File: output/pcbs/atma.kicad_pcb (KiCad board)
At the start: 2 copper layers, 99.8 x 100 mm, 24 parts

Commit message: more ergonomic 36-key version
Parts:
- moved ? 97.7 mm to (154.3, 172.4)
- moved _6 71.0 mm to (154.3, 172.4)
- moved _4 60.1 mm to (218.9, 123.8)
- moved _5 51.3 mm to (237.9, 171.4)
- moved ? 25.4 mm to (247.5, 121.9)
- moved S16 15.9 mm to (209.4, 181.0)
- moved S17 15.9 mm to (228.4, 181.0)
- moved S18 15.9 mm to (247.4, 181.0)
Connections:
- ? pad 1: matrix_pinky_bottom -> matrix_pinky_top
- ? pad 10: GP9 -> matrix_index_top
- ? pad 11: matrix_middle_top -> matrix_index_home
- ? pad 12: matrix_inner_bottom -> matrix_index_bottom
- ? pad 13: matrix_inner_home -> GP12
- ? pad 14: matrix_inner_top -> GP13
- ? pad 15: matrix_index_top -> matrix_inner_bottom
- ? pad 16: matrix_index_home -> matrix_inner_home
- ? pad 17: matrix_index_bottom -> matrix_inner_top
- ? pad 18: thumbfan_far_home -> thumbfan_near_home
- ? pad 20: thumbfan_near_home -> thumbfan_far_home
- ? pad 3: matrix_pinky_top -> matrix_pinky_bottom
- ? pad 4: matrix_ring_top -> matrix_ring_bottom
- ? pad 6: matrix_ring_bottom -> matrix_ring_top
- ? pad 7: matrix_middle_bottom -> matrix_middle_top
- ? pad 9: GP8 -> matrix_middle_bottom
- ? pad 3: GP8 -> GP12
- ? pad 4: GP8 -> GP12
- ? pad 5: GP9 -> GP13
- ? pad 6: GP9 -> GP13
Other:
- board size 99.8 x 100 mm -> 114.1 x 85.7 mm

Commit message: outline tweaks
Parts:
- removed _6: , MountingHole_2.2mm_M2_Pad_Via
- moved ? 35.2 mm to (247.5, 157.2)
- moved _5 19.6 mm to (218.9, 166.7)
- moved _3 19.1 mm to (161.9, 142.9)
- moved _4 19.0 mm to (199.9, 123.8)
- moved S16 4.76 mm to (209.4, 176.2)
- moved S17 4.76 mm to (228.4, 176.2)
- moved S18 4.76 mm to (247.4, 176.2)
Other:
- board size 114.1 x 85.7 mm -> 114.1 x 81 mm
- board text added: "JLCJLCJLCJLC"
- board text added: "atma v0.2.0"
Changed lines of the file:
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@@
           )
       (module MX (layer F.Cu)
-      (at 209.4 180.975 0)
+      (at 209.4 176.2125 0)
       (fp_text reference "S16" (at 0 0) (layer F.SilkS) hide (effects (font (size 1.27 1.27) (thickness 0.15))))
       (fp_text value "" (at 0 0) (layer F.SilkS) hide (effects (font (size 1.27 1.27) (thickness 0.15))))
@@
           )
       (module MX (layer F.Cu)
-      (at 228.4 180.975 0)
+      (at 228.4 176.2125 0)
       (fp_text reference "S17" (at 0 0) (layer F.SilkS) hide (effects (font (size 1.27 1.27) (thickness 0.15))))
       (fp_text value "" (at 0 0) (layer F.SilkS) hide (effects (font (size 1.27 1.27) (thickness 0.15))))
@@
           )
       (module MX (layer F.Cu)
-      (at 247.4 180.975 0)
+      (at 247.4 176.2125 0)
       (fp_text reference "S18" (at 0 0) (layer F.SilkS) hide (effects (font (size 1.27 1.27) (thickness 0.15))))
       (fp_text value "" (at 0 0) (layer F.SilkS) hide (effects (font (size 1.27 1.27) (thickness 0.15))))
@@
     )
     (module "44144-0003" (layer F.Cu)
-      (at 247.45000000000002 121.91999999999999 180)
+      (at 247.45000000000002 157.1625 180)
       (fp_line (start -7.62 0) (end 7.62 0) (layer F.Fab) (width 0.2))
       (fp_line (start 7.62 0) (end 7.62 16.89) (layer F.Fab) (width 0.2))
@@
     )
     (module "MountingHole_2.2mm_M2_Pad_Via" (version 20210722) (generator pcbnew) (layer "F.Cu")
-      (at 161.875 123.82499999999999 0)
+      (at 161.925 142.875 0)
       (fp_text reference "_3" (at 0 -3.2) (layer "F.SilkS") hide
         (effects (font (size 1 1) (thickness 0.15)))
@@
     )
     (module "MountingHole_2.2mm_M2_Pad_Via" (version 20210722) (generator pcbnew) (layer "F.Cu")
-      (at 218.925 123.82499999999999 0)
+      (at 199.925 123.82499999999999 0)
       (fp_text reference "_4" (at 0 -3.2) (layer "F.SilkS") hide
         (effects (font (size 1 1) (thickness 0.15)))
@@
     )
     (module "MountingHole_2.2mm_M2_Pad_Via" (version 20210722) (generator pcbnew) (layer "F.Cu")
-      (at 237.925 171.45 0)
+      (at 218.925 166.6875 0)
       (fp_text reference "_5" (at 0 -3.2) (layer "F.SilkS") hide
         (effects (font (size 1 1) (thickness 0.15)))
@@
       (pad "1" thru_hole circle locked (at 0 -1.65) (size 0.7 0.7) (drill 0.4) (layers *.Cu *.Mask))
     )
-    (module "MountingHole_2.2mm_M2_Pad_Via" (version 20210722) (generator pcbnew) (layer "F.Cu")
-      (at 154.305 172.4025 0)
-      (fp_text reference "_6" (at 0 -3.2) (layer "F.SilkS") hide
-        (effects (font (size 1 1) (thickness 0.15)))
-      )
-      (fp_circle (center 0 0) (end 2.45 0) (layer "F.CrtYd") (width 0.05) (fill none))
-      (pad "1" thru_hole circle locked (at 1.166726 1.166726) (size 0.7 0.7) (drill 0.4) (layers *.Cu *.Mask))
-      (pad "1" thru_hole circle locked (at 0 0) (size 4.4 4.4) (drill 2.2) (layers *.Cu *.Mask))
-      (pad "1" thru_hole circle locked (at 0 1.65) (size 0.7 0.7) (drill 0.4) (layers *.Cu *.Mask))
-      (pad "1" thru_hole circle locked (at 1.166726 -1.166726) (size 0.7 0.7) (drill 0.4) (layers *.Cu *.Mask))
-      (pad "1" thru_hole circle locked (at -1.65 0) (size 0.7 0.7) (drill 0.4) (layers *.Cu *.Mask))
-      (pad "1" thru_hole circle locked (at -1.166726 -1.166726) (size 0.7 0.7) (drill 0.4) (layers *.Cu *.Mask))
-      (pad "1" thru_hole circle locked (at -1.166726 1.166726) (size 0.7 0.7) (drill 0.4) (layers *.Cu *.Mask))
-      (pad "1" thru_hole circle locked (at 1.65 0) (size 0.7 0.7) (drill 0.4) (layers *.Cu *.Mask))
-      (pad "1" thru_hole circle locked (at 0 -1.65) (size 0.7 0.7) (drill 0.4) (layers *.Cu *.Mask))
-    )
-            (gr_line (start 142.875 182.97549871897368) (end 142.875 106.77499999999999) (angle 90) (layer Edge.Cuts) (width 0.15))
-(gr_line (start 144.875 104.77499999999999) (end 254.97383309877515 104.77499999999999) (angle 90) (layer Edge.Cuts) (width 0.15))
-(gr_line (start 256.97383279871684 106.77616660005879) (end 256.92616584041997 188.5011665999773) (angle 90) (layer Edge.Cuts) (width 0.15))
-(gr_line (start 254.9261661404783 190.5) (end 199.9750127766405 190.5) (angle 90) (layer Edge.Cuts) (width 0.15))
-(gr_line (start 199.77548676770925 190.49002248907823) (end 144.67547399106874 184.96552120805188) (angle 90) (layer Edge.Cuts) (width 0.15))
+            (gr_text "atma v0.2.0" (at 180.925 123.82499999999999 0) (layer F.SilkS)
+                (effects (font (size 1 1) (thickness 0.15)) )
+            )
+            (gr_text "JLCJLCJLCJLC" (at 180.925 142.875 0) (layer F.SilkS)
+                (effects (font (size 1 1) (thickness 0.15)) )
+            )
+            (gr_line (start 142.875 183.7375) (end 142.875 106.77499999999999) (angle 90) (layer Edge.Cuts) (width 0.15))
+(gr_line (start 144.875 104.77499999999999) (end 245.9413971571429 104.77499999999999) (angle 90) (layer Edge.Cuts) (width 0.15))
+(gr_line (start 247.8644450760108 106.22555776603781) (end 256.8977538164621 137.84213835761727) (angle 90) (layer Edge.Cuts) (width 0.15))
+(gr_line (start 256.97470479748904 138.39368039168767) (end 256.92709753301824 183.73959980011568) (angle 90) (layer Edge.Cuts) (width 0.15))
+(gr_line (start 144.875 185.7375) (end 254.92709863312336 185.7375) (angle 90) (layer Edge.Cuts) (width 0.15))
 (gr_arc (start 144.875 106.77499999999999) (end 144.875 104.77499999999999) (angle -90) (layer Edge.Cuts) (width 0.15))
-(gr_arc (start 254.97383309877515 106.77499999999999) (end 256.97383279877516 106.7761666) (angle -90.03342063109807) (layer Edge.Cuts) (width 0.15))
-(gr_arc (start 254.9261661404783 188.5) (end 254.9261661404783 190.5) (angle -89.96657937123672) (layer Edge.Cuts) (width 0.15))
-(gr_arc (start 199.9750127766405 188.5) (end 199.77548677664052 190.4900225) (angle -5.725523291754314) (layer Edge.Cuts) (width 0.15))
-(gr_arc (start 144.875 182.97549871897368) (end 142.875 182.97549871897368) (angle -84.27447670824557) (layer Edge.Cuts) (width 0.15))
+(gr_arc (start 245.9413971571429 106.77499999999999) (end 247.8644450571429 106.22555779999999) (angle -74.05460488609745) (layer Edge.Cuts) (width 0.15))
+(gr_arc (start 254.97470589759416 138.39158059157955) (end 256.97470479759414 138.39368039157955) (angle -16.00554996689867) (layer Edge.Cuts) (width 0.15))
+(gr_arc (start 254.92709863312336 183.73749999998836) (end 254.92709863312336 185.73749999998836) (angle -89.93984514645598) (layer Edge.Cuts) (width 0.15))
+(gr_arc (start 144.875 183.7375) (end 142.875 183.7375) (angle -90) (layer Edge.Cuts) (width 0.15))
 )

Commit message: outline tweaks, reroute
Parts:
- moved ? 2.86 mm to (247.5, 160.0)
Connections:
- ? pad 10: matrix_index_top -> matrix_index_bottom
- ? pad 12: matrix_index_bottom -> matrix_index_top
- ? pad 15: matrix_inner_bottom -> matrix_inner_top
- ? pad 17: matrix_inner_top -> matrix_inner_bottom
- ? pad 3: GP12 -> GP13
- ? pad 4: GP12 -> GP13
- ? pad 5: GP13 -> GP12
- ? pad 6: GP13 -> GP12
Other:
- outline, holes or cut-outs redrawn
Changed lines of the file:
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@@
       (pad 8 thru_hole oval (at 7.62 7.62 270) (size 2.5 1.5) (drill 1 (offset -0.5 0)) (layers *.Cu *.Mask) (net 9 "matrix_middle_home"))
       (pad 9 thru_hole oval (at 7.62 10.16 270) (size 2.5 1.5) (drill 1 (offset -0.5 0)) (layers *.Cu *.Mask) (net 8 "matrix_middle_bottom"))
-      (pad 10 thru_hole oval (at 5.08 10.16 180) (size 2.5 1.5) (drill 1 (offset -0.5 0)) (layers *.Cu *.Mask) (net 13 "matrix_index_top"))
+      (pad 10 thru_hole oval (at 5.08 10.16 180) (size 2.5 1.5) (drill 1 (offset -0.5 0)) (layers *.Cu *.Mask) (net 11 "matrix_index_bottom"))
       (pad 11 thru_hole oval (at 2.54 10.16 180) (size 2.5 1.5) (drill 1 (offset -0.5 0)) (layers *.Cu *.Mask) (net 12 "matrix_index_home"))
-      (pad 12 thru_hole oval (at 0 10.16 180) (size 2.5 1.5) (drill 1 (offset -0.5 0)) (layers *.Cu *.Mask) (net 11 "matrix_index_bottom"))
+      (pad 12 thru_hole oval (at 0 10.16 180) (size 2.5 1.5) (drill 1 (offset -0.5 0)) (layers *.Cu *.Mask) (net 13 "matrix_index_top"))
       (pad 13 thru_hole oval (at -2.54 10.16 180) (size 2.5 1.5) (drill 1 (offset -0.5 0)) (layers *.Cu *.Mask) (net 20 "GP12"))
       (pad 14 thru_hole oval (at -5.08 10.16 180) (size 2.5 1.5) (drill 1 (offset -0.5 0)) (layers *.Cu *.Mask) (net 21 "GP13"))
-      (pad 15 thru_hole oval (at -7.62 10.16 90) (size 2.5 1.5) (drill 1 (offset -0.5 0)) (layers *.Cu *.Mask) (net 14 "matrix_inner_bottom"))
+      (pad 15 thru_hole oval (at -7.62 10.16 90) (size 2.5 1.5) (drill 1 (offset -0.5 0)) (layers *.Cu *.Mask) (net 16 "matrix_inner_top"))
       (pad 16 thru_hole oval (at -7.62 7.62 90) (size 2.5 1.5) (drill 1 (offset -0.5 0)) (layers *.Cu *.Mask) (net 15 "matrix_inner_home"))
-      (pad 17 thru_hole oval (at -7.62 5.08 90) (size 2.5 1.5) (drill 1 (offset -0.5 0)) (layers *.Cu *.Mask) (net 16 "matrix_inner_top"))
+      (pad 17 thru_hole oval (at -7.62 5.08 90) (size 2.5 1.5) (drill 1 (offset -0.5 0)) (layers *.Cu *.Mask) (net 14 "matrix_inner_bottom"))
       (pad 18 thru_hole oval (at -7.62 2.54 90) (size 2.5 1.5) (drill 1 (offset -0.5 0)) (layers *.Cu *.Mask) (net 17 "thumbfan_near_home"))
       (pad 19 thru_hole oval (at -7.62 0 90) (size 2.5 1.5) (drill 1 (offset -0.5 0)) (layers *.Cu *.Mask) (net 18 "thumbfan_home_home"))
@@
     )
     (module "44144-0003" (layer F.Cu)
-      (at 247.45000000000002 157.1625 180)
+      (at 247.45000000000002 160.02 180)
       (fp_line (start -7.62 0) (end 7.62 0) (layer F.Fab) (width 0.2))
       (fp_line (start 7.62 0) (end 7.62 16.89) (layer F.Fab) (width 0.2))
@@
       (pad 1 smd rect (at -4.445 -0.83 180) (size 0.64 2.54) (layers F.Cu F.Paste F.Mask) (net 22 "3V3"))
       (pad 2 smd rect (at -3.175 -0.83 180) (size 0.64 2.54) (layers F.Cu F.Paste F.Mask) (net 2 "GND"))
-      (pad 3 smd rect (at -1.905 -0.83 180) (size 0.64 2.54) (layers F.Cu F.Paste F.Mask) (net 20 "GP12"))
-      (pad 4 smd rect (at -0.635 -0.83 180) (size 0.64 2.54) (layers F.Cu F.Paste F.Mask) (net 20 "GP12"))
-      (pad 5 smd rect (at 0.635 -0.83 180) (size 0.64 2.54) (layers F.Cu F.Paste F.Mask) (net 21 "GP13"))
-      (pad 6 smd rect (at 1.905 -0.83 180) (size 0.64 2.54) (layers F.Cu F.Paste F.Mask) (net 21 "GP13"))
+      (pad 3 smd rect (at -1.905 -0.83 180) (size 0.64 2.54) (layers F.Cu F.Paste F.Mask) (net 21 "GP13"))
+      (pad 4 smd rect (at -0.635 -0.83 180) (size 0.64 2.54) (layers F.Cu F.Paste F.Mask) (net 21 "GP13"))
+      (pad 5 smd rect (at 0.635 -0.83 180) (size 0.64 2.54) (layers F.Cu F.Paste F.Mask) (net 20 "GP12"))
+      (pad 6 smd rect (at 1.905 -0.83 180) (size 0.64 2.54) (layers F.Cu F.Paste F.Mask) (net 20 "GP12"))
       (pad 7 smd rect (at 3.175 -0.83 180) (size 0.64 2.54) (layers F.Cu F.Paste F.Mask) (net 2 "GND"))
       (pad 8 smd rect (at 4.445 -0.83 180) (size 0.64 2.54) (layers F.Cu F.Paste F.Mask) (net 22 "3V3"))
@@
       (pad 1 smd rect (at -4.445 -0.83 180) (size 0.64 2.54) (layers B.Cu B.Paste B.Mask) (net 22 "3V3"))
       (pad 2 smd rect (at -3.175 -0.83 180) (size 0.64 2.54) (layers B.Cu B.Paste B.Mask) (net 2 "GND"))
-      (pad 3 smd rect (at -1.905 -0.83 180) (size 0.64 2.54) (layers B.Cu B.Paste B.Mask) (net 20 "GP12"))
-      (pad 4 smd rect (at -0.635 -0.83 180) (size 0.64 2.54) (layers B.Cu B.Paste B.Mask) (net 20 "GP12"))
-      (pad 5 smd rect (at 0.635 -0.83 180) (size 0.64 2.54) (layers B.Cu B.Paste B.Mask) (net 21 "GP13"))
-      (pad 6 smd rect (at 1.905 -0.83 180) (size 0.64 2.54) (layers B.Cu B.Paste B.Mask) (net 21 "GP13"))
+      (pad 3 smd rect (at -1.905 -0.83 180) (size 0.64 2.54) (layers B.Cu B.Paste B.Mask) (net 21 "GP13"))
+      (pad 4 smd rect (at -0.635 -0.83 180) (size 0.64 2.54) (layers B.Cu B.Paste B.Mask) (net 21 "GP13"))
+      (pad 5 smd rect (at 0.635 -0.83 180) (size 0.64 2.54) (layers B.Cu B.Paste B.Mask) (net 20 "GP12"))
+      (pad 6 smd rect (at 1.905 -0.83 180) (size 0.64 2.54) (layers B.Cu B.Paste B.Mask) (net 20 "GP12"))
       (pad 7 smd rect (at 3.175 -0.83 180) (size 0.64 2.54) (layers B.Cu B.Paste B.Mask) (net 2 "GND"))
       (pad 8 smd rect (at 4.445 -0.83 180) (size 0.64 2.54) (layers B.Cu B.Paste B.Mask) (net 22 "3V3"))
@@
                 (effects (font (size 1 1) (thickness 0.15)) )
             )
-            (gr_line (start 142.875 183.7375) (end 142.875 106.77499999999999) (angle 90) (layer Edge.Cuts) (width 0.15))
-(gr_line (start 144.875 104.77499999999999) (end 245.9413971571429 104.77499999999999) (angle 90) (layer Edge.Cuts) (width 0.15))
-(gr_line (start 247.8644450760108 106.22555776603781) (end 256.8977538164621 137.84213835761727) (angle 90) (layer Edge.Cuts) (width 0.15))
-(gr_line (start 256.97470479748904 138.39368039168767) (end 256.92709753301824 183.73959980011568) (angle 90) (layer Edge.Cuts) (width 0.15))
-(gr_line (start 144.875 185.7375) (end 254.92709863312336 185.7375) (angle 90) (layer Edge.Cuts) (width 0.15))
-(gr_arc (start 144.875 106.77499999999999) (end 144.875 104.77499999999999) (angle -90) (layer Edge.Cuts) (width 0.15))
-(gr_arc (start 245.9413971571429 106.77499999999999) (end 247.8644450571429 106.22555779999999) (angle -74.05460488609745) (layer Edge.Cuts) (width 0.15))
-(gr_arc (start 254.97470589759416 138.39158059157955) (end 256.97470479759414 138.39368039157955) (angle -16.00554996689867) (layer Edge.Cuts) (width 0.15))
-(gr_arc (start 254.92709863312336 183.73749999998836) (end 254.92709863312336 185.73749999998836) (angle -89.93984514645598) (layer Edge.Cuts) (width 0.15))
-(gr_arc (start 144.875 183.7375) (end 142.875 183.7375) (angle -90) (layer Edge.Cuts) (width 0.15))
+            (gr_line (start 142.875 182.7375) (end 142.875 107.77499999999999) (angle 90) (layer Edge.Cuts) (width 0.15))
+(gr_line (start 145.875 104.77499999999999) (end 245.1870958 104.77499999999999) (angle 90) (layer Edge.Cuts) (width 0.15))
+(gr_line (start 248.07166761886796 106.95083666603784) (end 256.8591307152592 137.70695750340712) (angle 90) (layer Edge.Cuts) (width 0.15))
+(gr_line (start 256.9745571962861 138.53427053746418) (end 256.9281462995275 182.74064970004838) (angle 90) (layer Edge.Cuts) (width 0.15))
+(gr_line (start 145.875 185.7375) (end 253.92814799963259 185.7375) (angle 90) (layer Edge.Cuts) (width 0.15))
+(gr_arc (start 145.875 107.77499999999999) (end 145.875 104.77499999999999) (angle -90) (layer Edge.Cuts) (width 0.15))
+(gr_arc (start 245.1870958 107.77499999999999) (end 248.0716677 106.9508367) (angle -74.05460488609751) (layer Edge.Cuts) (width 0.15))
+(gr_arc (start 253.97455889639124 138.53112083736926) (end 256.97455719639123 138.53427053736925) (angle -16.005549966613025) (layer Edge.Cuts) (width 0.15))
+(gr_arc (start 253.92814799963259 182.73749999998836) (end 253.92814799963259 185.73749999998836) (angle -89.93984514795574) (layer Edge.Cuts) (width 0.15))
+(gr_arc (start 145.875 182.7375) (end 142.875 182.7375) (angle -90) (layer Edge.Cuts) (width 0.15))
 )

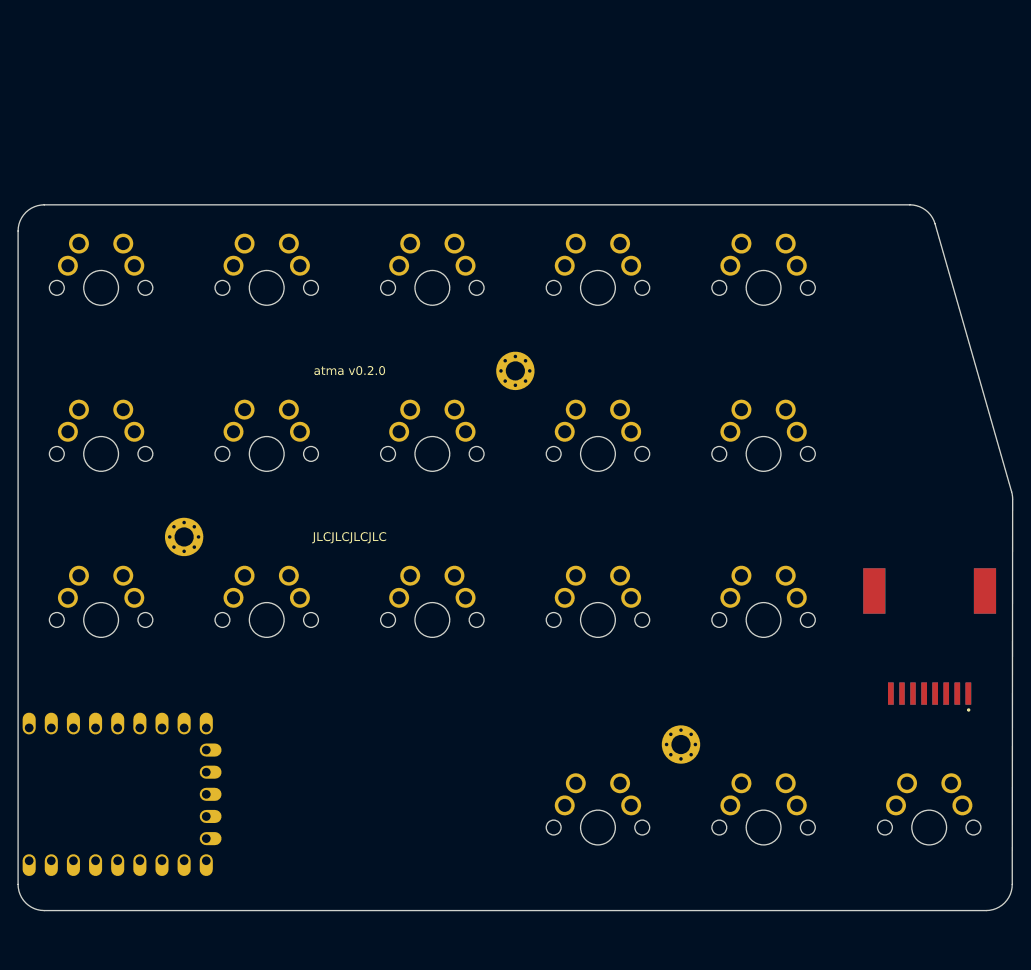
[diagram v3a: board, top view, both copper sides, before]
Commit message: small outline tweak
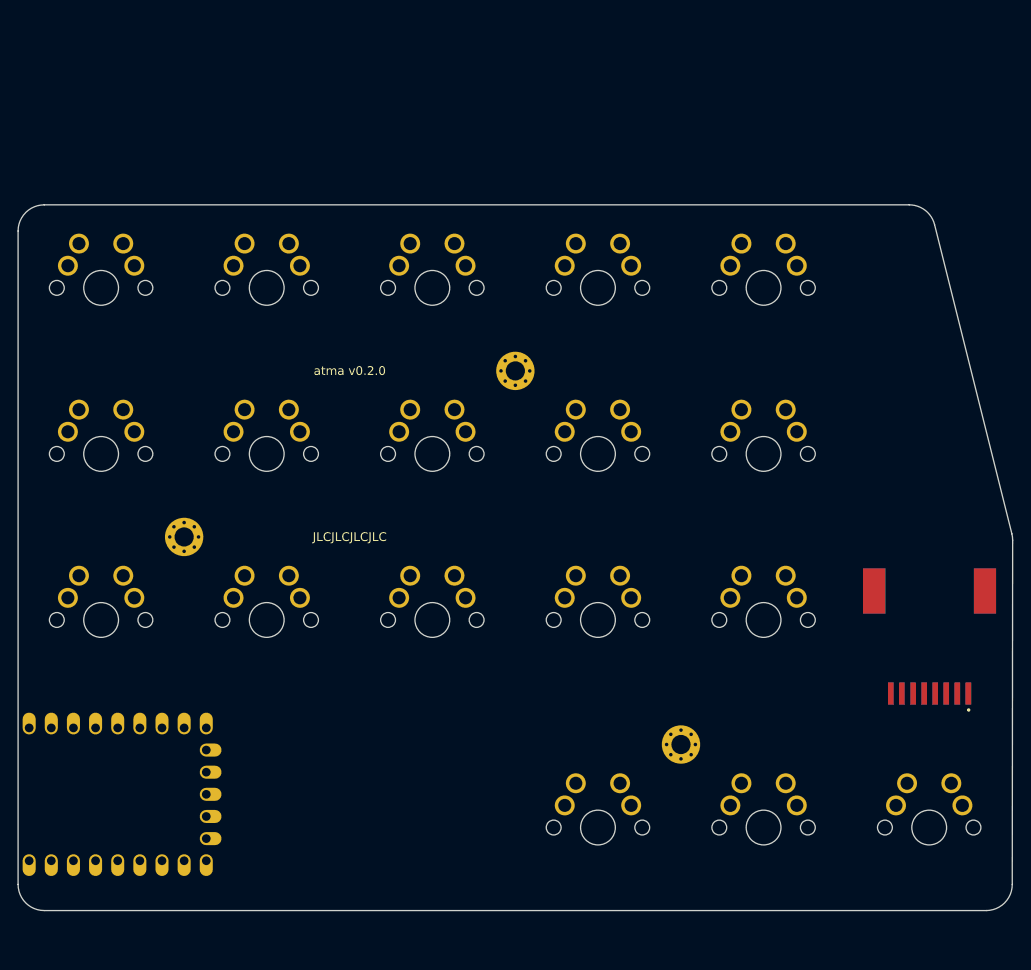
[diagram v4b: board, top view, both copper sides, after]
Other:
- outline, holes or cut-outs redrawn
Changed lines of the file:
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@@
             )
             (gr_line (start 142.875 182.7375) (end 142.875 107.77499999999999) (angle 90) (layer Edge.Cuts) (width 0.15))
-(gr_line (start 145.875 104.77499999999999) (end 245.1870958 104.77499999999999) (angle 90) (layer Edge.Cuts) (width 0.15))
-(gr_line (start 248.07166761886796 106.95083666603784) (end 256.8591307152592 137.70695750340712) (angle 90) (layer Edge.Cuts) (width 0.15))
-(gr_line (start 256.9745571962861 138.53427053746418) (end 256.9281462995275 182.74064970004838) (angle 90) (layer Edge.Cuts) (width 0.15))
-(gr_line (start 145.875 185.7375) (end 253.92814799963259 185.7375) (angle 90) (layer Edge.Cuts) (width 0.15))
+(gr_line (start 145.875 104.77499999999999) (end 245.107670775 104.77499999999999) (angle 90) (layer Edge.Cuts) (width 0.15))
+(gr_line (start 248.01809829852945 107.04739319411772) (end 256.8849966358661 142.51498654346437) (angle 90) (layer Edge.Cuts) (width 0.15))
+(gr_line (start 256.97456711245326 143.24609284946928) (end 256.9284954803149 182.74099950006348) (angle 90) (layer Edge.Cuts) (width 0.15))
+(gr_line (start 145.875 185.7375) (end 253.92849748019836 185.7375) (angle 90) (layer Edge.Cuts) (width 0.15))
 (gr_arc (start 145.875 107.77499999999999) (end 145.875 104.77499999999999) (angle -90) (layer Edge.Cuts) (width 0.15))
-(gr_arc (start 245.1870958 107.77499999999999) (end 248.0716677 106.9508367) (angle -74.05460488609751) (layer Edge.Cuts) (width 0.15))
-(gr_arc (start 253.97455889639124 138.53112083736926) (end 256.97455719639123 138.53427053736925) (angle -16.005549966613025) (layer Edge.Cuts) (width 0.15))
-(gr_arc (start 253.92814799963259 182.73749999998836) (end 253.92814799963259 185.73749999998836) (angle -89.93984514795574) (layer Edge.Cuts) (width 0.15))
+(gr_arc (start 245.107670775 107.77499999999999) (end 248.018098275 107.04739319999999) (angle -75.96375792170193) (layer Edge.Cuts) (width 0.15))
+(gr_arc (start 253.97456911233672 143.24259334934675) (end 256.97456711233673 143.24609284934675) (angle -14.103077621681855) (layer Edge.Cuts) (width 0.15))
+(gr_arc (start 253.92849748019836 182.73749999998836) (end 253.92849748019836 185.73749999998836) (angle -89.93316445752373) (layer Edge.Cuts) (width 0.15))
 (gr_arc (start 145.875 182.7375) (end 142.875 182.7375) (angle -90) (layer Edge.Cuts) (width 0.15))
 )
